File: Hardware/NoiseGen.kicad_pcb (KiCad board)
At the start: 2 copper layers, 78.7 x 33 mm, 25 parts, among them J1 CONN_01X02, J2 SMA, Q1 BFR92, SW1 SPST, U1 MAX2650, U2 AP2210, U3 MAX2650

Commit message: Added text to PCB, cleaned up PCB
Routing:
- net GND: track 464.5 -> 466.6 mm
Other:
- rule pad_to_mask_clearance: 0.2 -> 0.1016
- board text added: "NoiseGen"
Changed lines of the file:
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@@
     (area 55.508822 84.989999 202.724286 129.745001)
     (thickness 1.6)
-    (drawings 12)
-    (tracks 369)
+    (drawings 11)
+    (tracks 372)
     (zones 0)
     (modules 25)
@@
   (page A4)
   (layers
-    (0 F.Cu signal hide)
-    (31 B.Cu signal hide)
+    (0 F.Cu signal)
+    (31 B.Cu signal)
     (32 B.Adhes user)
     (33 F.Adhes user)
@@
   )
   (setup
-    (last_trace_width 1.016)
+    (last_trace_width 0.508)
     (user_trace_width 0.1524)
     (user_trace_width 0.2032)
@@
     (pad_size 1.524 1.524)
     (pad_drill 0.762)
-    (pad_to_mask_clearance 0.2)
+    (pad_to_mask_clearance 0.1016)
+    (pad_to_paste_clearance_ratio -0.025)
     (aux_axis_origin 0 0)
-    (visible_elements FFFFE77F)
+    (visible_elements 7FFFFFFF)
     (pcbplotparams
       (layerselection 0x00030_ffffffff)
@@
     )
   )
+  (gr_text NoiseGen (at 137.16 111.76) (layer F.SilkS)
+    (effects (font (size 2.794 2.794) (thickness 0.381)))
+  )
   (dimension 78.74 (width 0.3) (layer Eco1.User)
     (gr_text "3.1000 in" (at 110.49 128.35) (layer Eco1.User)
@@
     (arrow2b (pts (xy 71.12 127) (xy 72.246504 126.413579)))
   )
-  (gr_line (start 74.295 95.25) (end 74.295 95.25) (layer F.SilkS) (width 0.2))
-  (gr_line (start 73.025 95.25) (end 74.295 95.25) (layer F.SilkS) (width 0.381))
-  (gr_line (start 73.66 94.615) (end 73.66 94.615) (layer F.SilkS) (width 0.2))
-  (gr_line (start 73.66 95.885) (end 73.66 94.615) (layer F.SilkS) (width 0.381))
+  (gr_line (start 73.025 92.329) (end 74.295 92.329) (layer F.SilkS) (width 0.381))
+  (gr_line (start 73.66 92.964) (end 73.66 91.694) (layer F.SilkS) (width 0.381))
   (gr_text "Coplanar wave guide with ground plane:\n40 mil trace\n8 mil gap\nZ0: 51.3865 Ohms\nAng: 0.0834 Rad" (at 156.21 101.6) (layer Cmts.User)
     (effects (font (size 1.5 1.5) (thickness 0.3)) (justify left))
@@
   (segment (start 76.2 103.8352) (end 74.549001 105.486199) (width 1.016) (layer F.Cu) (net 1) (status 10))
   (segment (start 74.549001 105.486199) (end 73.583801 105.486199) (width 1.016) (layer F.Cu) (net 1))
+  (segment (start 128.204 97.856) (end 128.27 97.79) (width 0.508) (layer F.Cu) (net 2))
+  (segment (start 128.27 97.79) (end 128.27 97.155) (width 0.508) (layer F.Cu) (net 2))
+  (segment (start 126.83 97.856) (end 128.204 97.856) (width 0.508) (layer F.Cu) (net 2))
   (segment (start 80.264 91.424) (end 80.264 91.694) (width 1.016) (layer F.Cu) (net 2))
   (via (at 81.28 92.71) (size 0.8) (drill 0.4) (layers F.Cu B.Cu) (net 2))

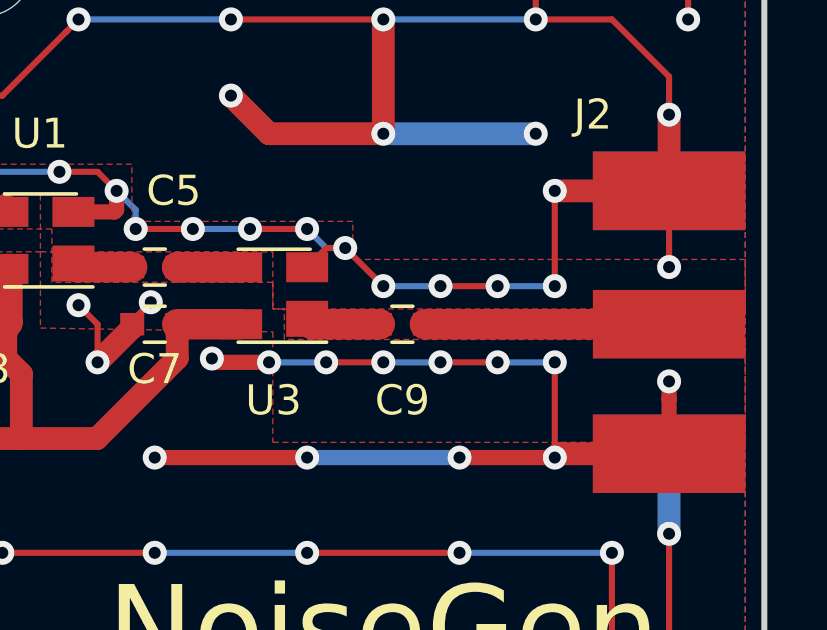
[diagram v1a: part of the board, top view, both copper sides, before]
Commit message: Add TVS diode
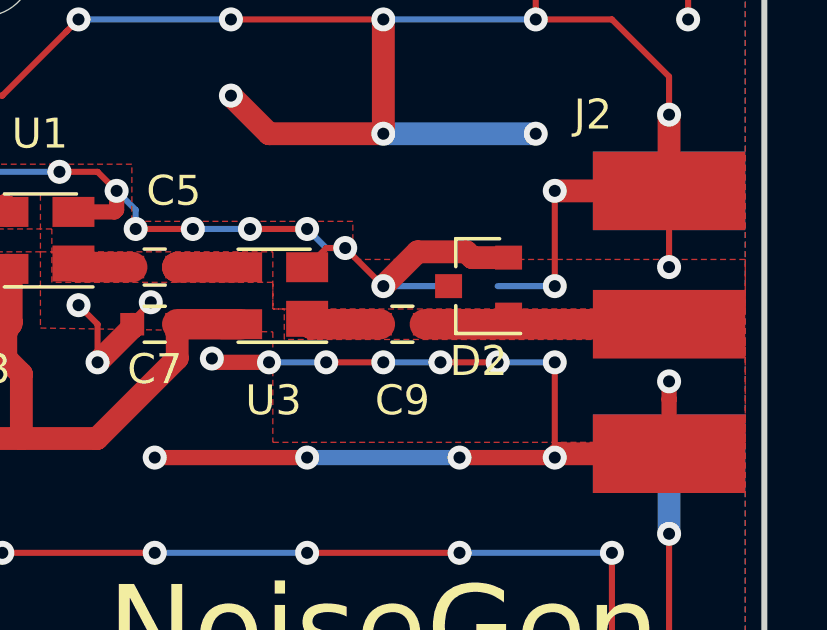
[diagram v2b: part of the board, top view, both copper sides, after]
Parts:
- added D2: CM1214A, TO_SOT_Packages_SMD:SOT-23, F.Cu at (140.3, 100.3)
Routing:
- net Net-(C9-Pad1): track 8.14 -> 11.5 mm
- net GND: track 466.6 -> 469.4 mm, vias 118 -> 116
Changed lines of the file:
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@@
 (kicad_pcb (version 20170123) (host pcbnew "(2017-05-02 revision e4d2924ee)-makepkg")
   (general
-    (links 48)
+    (links 50)
     (no_connects 1)
     (area 55.508822 84.989999 202.724286 129.745001)
     (thickness 1.6)
     (drawings 11)
-    (tracks 372)
+    (tracks 377)
     (zones 0)
-    (modules 25)
+    (modules 26)
     (nets 16)
   )
@@
   )
   (setup
-    (last_trace_width 0.508)
+    (last_trace_width 0.762)
     (user_trace_width 0.1524)
     (user_trace_width 0.2032)
@@
     )
   )
+  (module TO_SOT_Packages_SMD:SOT-23 (layer F.Cu)
+    (at 140.335 100.33 180)
+    (descr "SOT-23, Standard")
+    (tags SOT-23)
+    (attr smd)
+    (fp_text reference D2 (at 0 -2.5 180) (layer F.SilkS)
+      (effects (font (size 1 1) (thickness 0.15)))
+    )
+    (fp_text value CM1214A (at 0 2.5 180) (layer F.Fab)
+      (effects (font (size 1 1) (thickness 0.15)))
+    )
+    (fp_line (start 0.76 1.58) (end -0.7 1.58) (layer F.SilkS) (width 0.12))
+    (fp_line (start 0.76 -1.58) (end -1.4 -1.58) (layer F.SilkS) (width 0.12))
+    (fp_line (start -1.7 1.75) (end -1.7 -1.75) (layer F.CrtYd) (width 0.05))
+    (fp_line (start 1.7 1.75) (end -1.7 1.75) (layer F.CrtYd) (width 0.05))
+    (fp_line (start 1.7 -1.75) (end 1.7 1.75) (layer F.CrtYd) (width 0.05))
+    (fp_line (start -1.7 -1.75) (end 1.7 -1.75) (layer F.CrtYd) (width 0.05))
+    (fp_line (start 0.76 -1.58) (end 0.76 -0.65) (layer F.SilkS) (width 0.12))
+    (fp_line (start 0.76 1.58) (end 0.76 0.65) (layer F.SilkS) (width 0.12))
+    (fp_line (start -0.7 1.52) (end 0.7 1.52) (layer F.Fab) (width 0.1))
+    (fp_line (start 0.7 -1.52) (end 0.7 1.52) (layer F.Fab) (width 0.1))
+    (fp_line (start -0.7 -0.95) (end -0.15 -1.52) (layer F.Fab) (width 0.1))
+    (fp_line (start -0.15 -1.52) (end 0.7 -1.52) (layer F.Fab) (width 0.1))
+    (fp_line (start -0.7 -0.95) (end -0.7 1.5) (layer F.Fab) (width 0.1))
+    (fp_text user %R (at 0 0 270) (layer F.Fab)
+      (effects (font (size 0.5 0.5) (thickness 0.075)))
+    )
+    (pad 3 smd rect (at 1 0 180) (size 0.9 0.8) (layers F.Cu F.Paste F.Mask))
+    (pad 2 smd rect (at -1 0.95 180) (size 0.9 0.8) (layers F.Cu F.Paste F.Mask)
+      (net 2 GND))
+    (pad 1 smd rect (at -1 -0.95 180) (size 0.9 0.8) (layers F.Cu F.Paste F.Mask)
+      (net 12 "Net-(C9-Pad1)"))
+    (model ${KISYS3DMOD}/TO_SOT_Packages_SMD.3dshapes/SOT-23.wrl
+      (at (xyz 0 0 0))
+      (scale (xyz 1 1 1))
+      (rotate (xyz 0 0 0))
+    )
+  )
   (gr_text NoiseGen (at 137.16 111.76) (layer F.SilkS)
     (effects (font (size 2.794 2.794) (thickness 0.381)))
@@
   (segment (start 76.2 103.8352) (end 74.549001 105.486199) (width 1.016) (layer F.Cu) (net 1) (status 10))
   (segment (start 74.549001 105.486199) (end 73.583801 105.486199) (width 1.016) (layer F.Cu) (net 1))
+  (segment (start 141.335 99.38) (end 140.123 99.38) (width 0.762) (layer F.Cu) (net 2))
+  (segment (start 140.123 99.38) (end 139.93 99.187) (width 0.762) (layer F.Cu) (net 2))
+  (segment (start 139.93 99.187) (end 138.303 99.187) (width 0.762) (layer F.Cu) (net 2))
+  (segment (start 138.303 99.187) (end 137.16 100.33) (width 0.762) (layer F.Cu) (net 2))
   (segment (start 128.204 97.856) (end 128.27 97.79) (width 0.508) (layer F.Cu) (net 2))
   (segment (start 128.27 97.79) (end 128.27 97.155) (width 0.508) (layer F.Cu) (net 2))
@@
   (segment (start 139.065 100.33) (end 137.16 100.33) (width 0.2032) (layer B.Cu) (net 2))
   (via (at 137.16 100.33) (size 0.8) (drill 0.4) (layers F.Cu B.Cu) (net 2))
-  (segment (start 140.97 100.33) (end 139.065 100.33) (width 0.2032) (layer F.Cu) (net 2))
-  (via (at 139.065 100.33) (size 0.8) (drill 0.4) (layers F.Cu B.Cu) (net 2))
   (segment (start 142.875 100.33) (end 140.97 100.33) (width 0.2032) (layer B.Cu) (net 2))
-  (via (at 140.97 100.33) (size 0.8) (drill 0.4) (layers F.Cu B.Cu) (net 2))
   (segment (start 142.875 97.155) (end 142.875 100.33) (width 0.2032) (layer F.Cu) (net 2))
   (via (at 142.875 100.33) (size 0.8) (drill 0.4) (layers F.Cu B.Cu) (net 2))
@@
   (segment (start 137.045 101.6) (end 134.8 101.6) (width 1.016) (layer F.Cu) (net 11) (status 30))
   (segment (start 134.8 101.6) (end 134.62 101.42) (width 1.016) (layer F.Cu) (net 11) (status 30))
+  (segment (start 138.545 101.6) (end 141.015 101.6) (width 0.762) (layer F.Cu) (net 12))
+  (segment (start 141.015 101.6) (end 141.335 101.28) (width 0.762) (layer F.Cu) (net 12))
+  (segment (start 141.335 101.28) (end 141.335 101.33) (width 0.762) (layer F.Cu) (net 12))
+  (segment (start 141.335 101.33) (end 141.605 101.6) (width 0.762) (layer F.Cu) (net 12))
   (segment (start 146.685 101.6) (end 138.545 101.6) (width 1.016) (layer F.Cu) (net 12) (status 30))
   (segment (start 75.946 89.574) (end 80.114 89.574) (width 0.762) (layer F.Cu) (net 13) (status 30))
